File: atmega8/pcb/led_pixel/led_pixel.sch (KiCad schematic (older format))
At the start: 68 parts, among them IC1 ATMEGA8-AI, P1 USB_OTG, P10 CONN_01X04, P2 RESET, P3 CONN_01X03, P4 MOSI, P5 MISO, P6 SCK, P7 CONN_01X03, P8 5V, P9 GND, U1 MC78M05CDT, U2 PT4115, U3 PT4115, U4 SN75176, U5 PT4115, Y1 CRYSTAL

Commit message: layout in process... :|
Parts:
- removed C7: 100n, Capacitors_SMD:C_0603_HandSoldering, symbol C
- removed JP2: DMX_ADR_0, proz_jumper:solderjumper, symbol JUMPER_NO_Small
- removed JP3: DMX_ADR_1, proz_jumper:solderjumper, symbol JUMPER_NO_Small
- removed JP4: DMX_ADR_2, proz_jumper:solderjumper, symbol JUMPER_NO_Small
- removed JP5: DMX_ADR_3, proz_jumper:solderjumper, symbol JUMPER_NO_Small
- removed JP6: DMX_ADR_4, proz_jumper:solderjumper, symbol JUMPER_NO_Small
- removed JP7: DMX_ADR_5, proz_jumper:solderjumper, symbol JUMPER_NO_Small
- removed JP8: DMX_ADR_6, proz_jumper:solderjumper, symbol JUMPER_NO_Small
- removed JP9: DMX_ADR_7, proz_jumper:solderjumper, symbol JUMPER_NO_Small
- removed P2: RESET, Socket_Strips:Socket_Strip_Straight_1x01, symbol CONN_01X01
- removed P4: MOSI, Socket_Strips:Socket_Strip_Straight_1x01, symbol CONN_01X01
- removed P5: MISO, Socket_Strips:Socket_Strip_Straight_1x01, symbol CONN_01X01
- removed P6: SCK, Socket_Strips:Socket_Strip_Straight_1x01, symbol CONN_01X01
- removed P8: 5V, Socket_Strips:Socket_Strip_Straight_1x01, symbol CONN_01X01
- removed P9: GND, Socket_Strips:Socket_Strip_Straight_1x01, symbol CONN_01X01
- added P2: ISP, Connectors:IDC_Header_Straight_6pins, symbol CONN_02X03
- added SW1: SW_DIP_x08, proz_switch:SW_DIP_x8_SMD_2.54, symbol SW_DIP_x08
- renumbered C11 to C10, C12 to C11, C13 to C12, C14 to C13, C15 to C14, C8 to C7, C9 to C8, C10 to C9, D6 to D5, D5 to D6, P7 to P4, P10 to P5
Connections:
- net +5V: now also P2.2 (P2)
- net GND: now also P2.6 (P6), SW1.1, SW1.2, SW1.3, SW1.4, SW1.5, SW1.6, SW1.7, SW1.8
- net LED_B: now also P2.1 (P1)
- net LED_G: now also P2.4 (P4)
- net SCK: now reaches IC1.17 ((SCK)PB5)
- net SCK: now also P2.3 (P3)
- net DMX_6: now reaches IC1.2 ((XCK/T0)PD4)
- net DMX_6: now also SW1.10
- net DMX_0: now reaches IC1.23 ((ADC0)PC0)
- net DMX_0: now also SW1.16
- net DMX_1: now reaches IC1.24 ((ADC1)PC1)
- net DMX_1: now also SW1.15
- net DMX_2: now reaches IC1.25 ((ADC2)PC2)
- net DMX_2: now also SW1.14
- net DMX_3: now reaches IC1.26 ((ADC3)PC3)
- net DMX_3: now also SW1.13
- net DMX_4: now reaches IC1.27 ((ADC4/SDA)PC4)
- net DMX_4: now also SW1.12
- net DMX_5: now reaches IC1.28 ((ADC5/SCL)PC5), P3.1 (P1)
- net DMX_5: now also SW1.11
- net RESET: now reaches C4.1, IC1.29 (PC6(~RESET~)), R4.2
- net RESET: now also P2.5 (P5)
- net DMX_7: now reaches IC1.9 ((T1)PD5)
- net DMX_7: now also SW1.9
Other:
- moved on the sheet: C10, C7, C8, C9, D3, D6, P4, R7, R8, U1

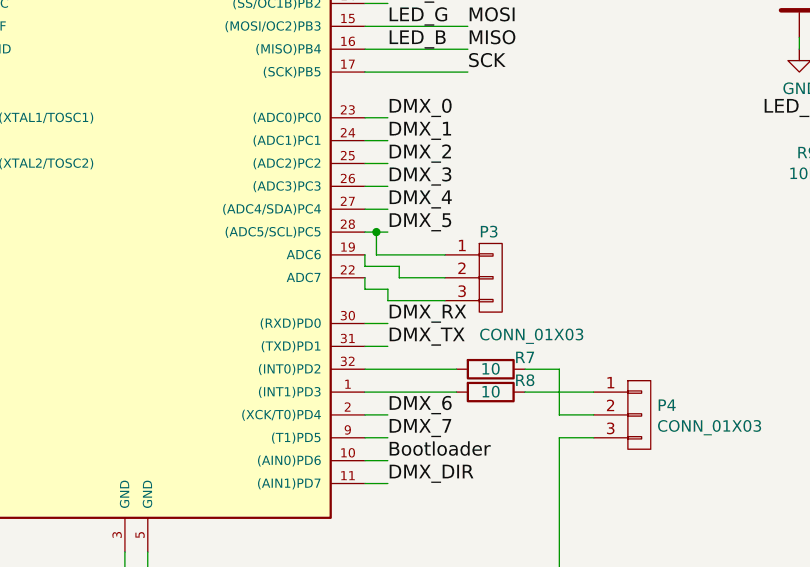
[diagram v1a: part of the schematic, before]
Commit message: finished first shot of the layout...
there are mounting holes missing...
...so what ;)
I hope to find a place for them this week...
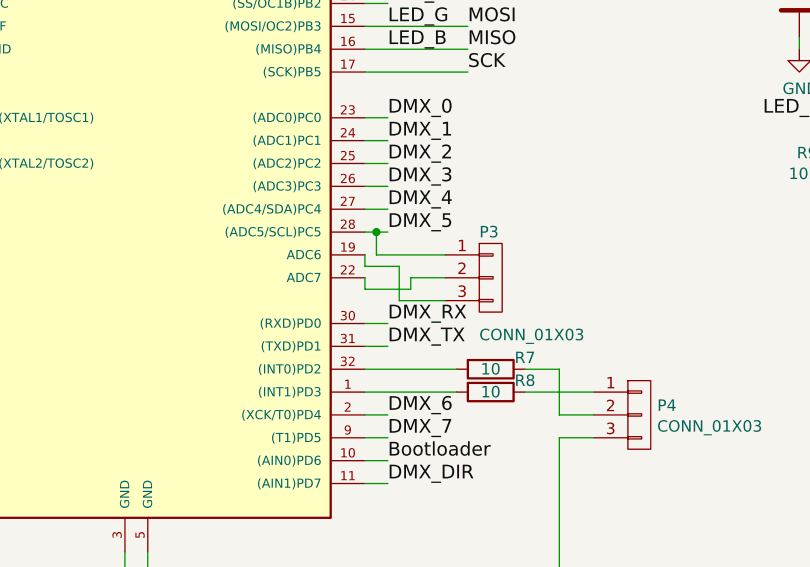
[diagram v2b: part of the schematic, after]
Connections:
- net at IC1.19 (ADC6): now also P3.3 (P3); no longer P3.2 (P2)
- net at IC1.22 (ADC7): now also P3.2 (P2); no longer P3.3 (P3)
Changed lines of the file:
@@
 	4150 5650 4300 5650
 Wire Wire Line
-	4300 5650 4300 5700
-Wire Wire Line
-	4300 5700 4500 5700
-Wire Wire Line
 	4150 5700 4150 5750
 Wire Wire Line
-	4150 5750 4250 5750
-Wire Wire Line
-	4250 5750 4250 5800
-Wire Wire Line
-	4250 5800 4500 5800
+	4150 5750 4350 5750
 Wire Wire Line
 	5000 7100 5000 6400
@@
 Wire Wire Line
 	5700 1400 5050 1400
+Wire Wire Line
+	4350 5750 4350 5700
+Wire Wire Line
+	4350 5700 4500 5700
+Wire Wire Line
+	4300 5650 4300 5800
+Wire Wire Line
+	4300 5800 4500 5800
 $EndSCHEMATC

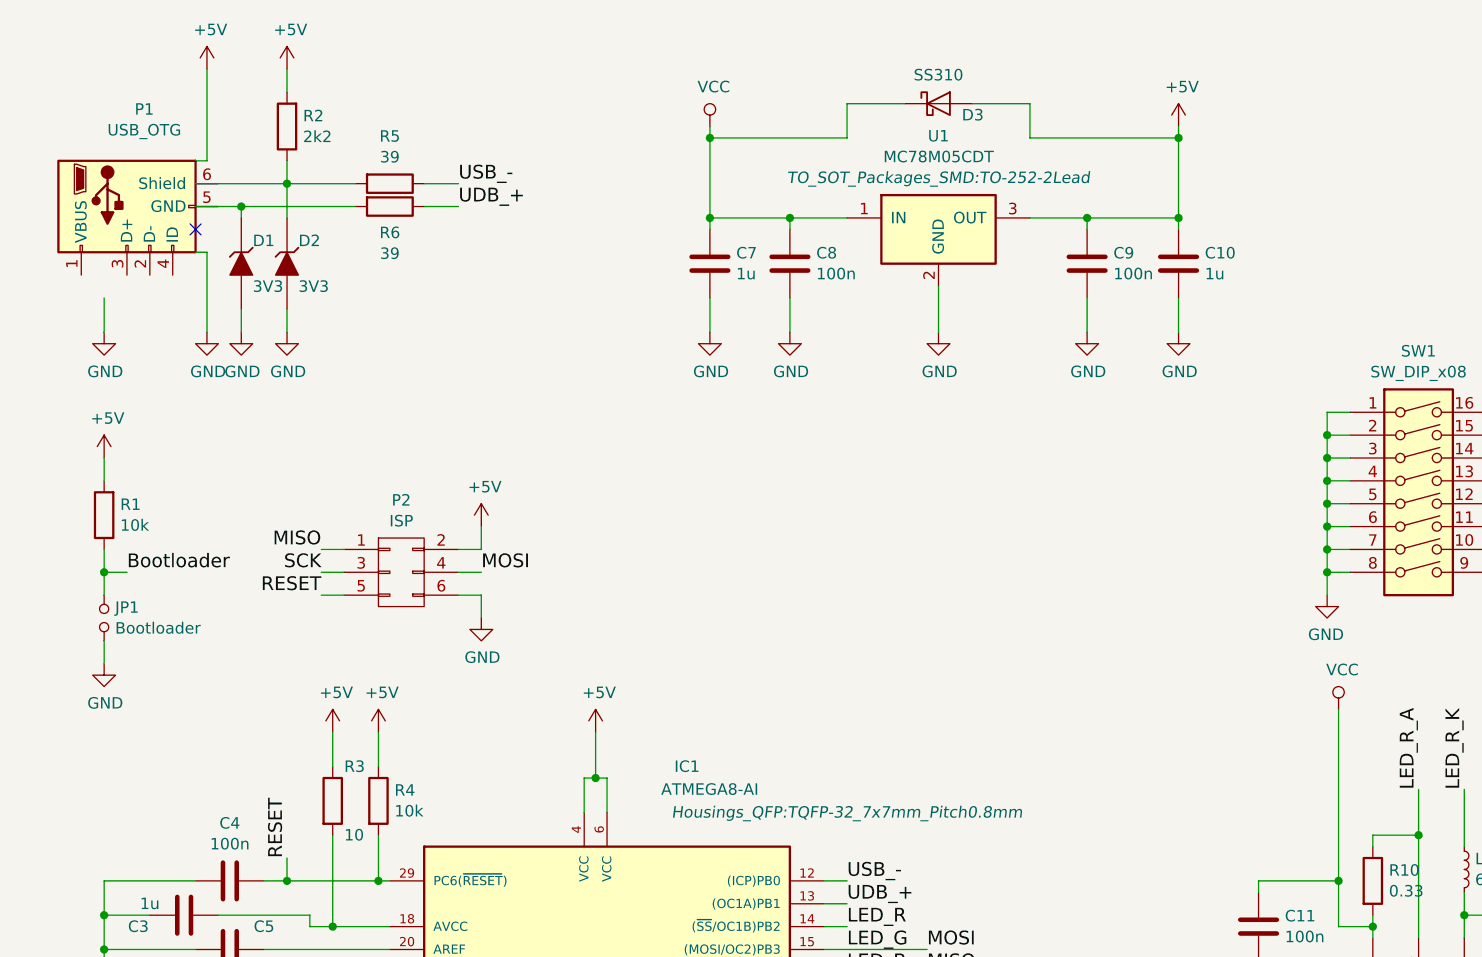
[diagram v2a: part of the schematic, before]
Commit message: finished rought layout with mounting holes and needle debug adaptor...
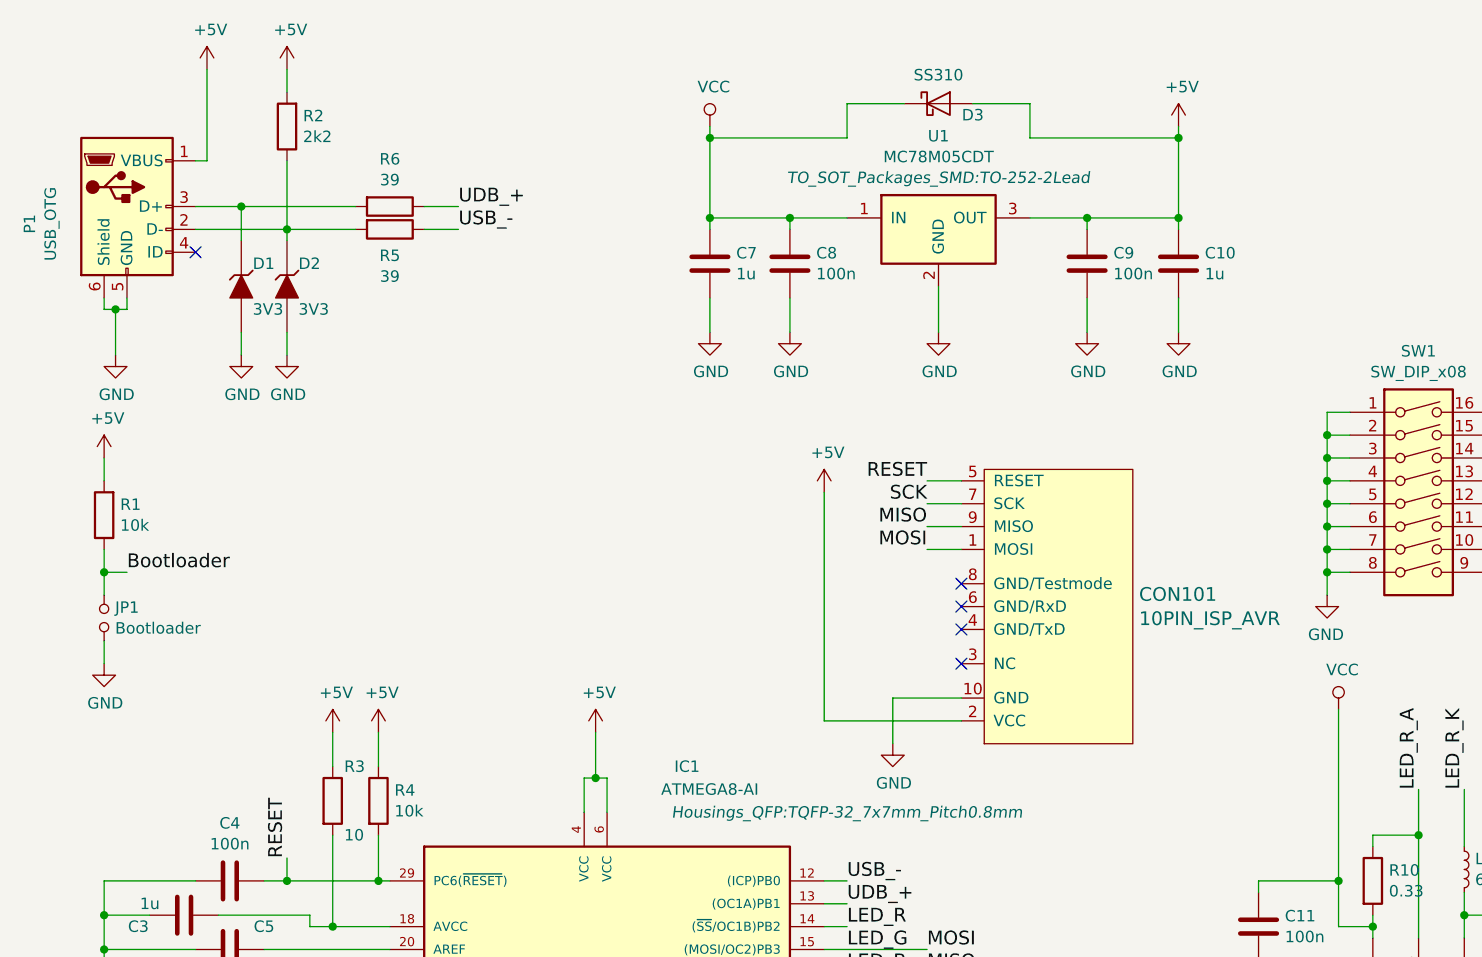
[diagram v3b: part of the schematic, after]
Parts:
- removed P2: ISP, Connectors:IDC_Header_Straight_6pins, symbol CONN_02X03
- added CON101: 10PIN_ISP_AVR, proz_connectors:TC2050-IDC, symbol 10PIN_ISP_AVR
- D1, D2: footprint Diodes_SMD:MiniMELF_Handsoldering -> Diodes_SMD:D_MiniMELF_Standard
- D3, D4, D5, D7, D8: footprint Diodes_SMD:SMA_Handsoldering -> Diodes_SMD:D_SMA_Standard
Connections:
- net +5V: now also P1.1 (VBUS), CON101.2 (VCC)
- net GND: now also P1.5 (GND), P1.6 (Shield), CON101.10 (GND)
- net LED_B: now also CON101.9 (MISO)
- net LED_G: now also CON101.1 (MOSI)
- net RESET: now also CON101.5 (RESET)
- net SCK: now also CON101.7 (SCK)
- net at P1.2 (D-): now also D2.1 (K), R2.1, R5.2
- net at P1.3 (D+): now also D1.1 (K), R6.2
- no-connect marks 1 -> 5
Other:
- moved on the sheet: D1, D2, R5
